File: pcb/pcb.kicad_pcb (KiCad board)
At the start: 2 copper layers, 2 parts

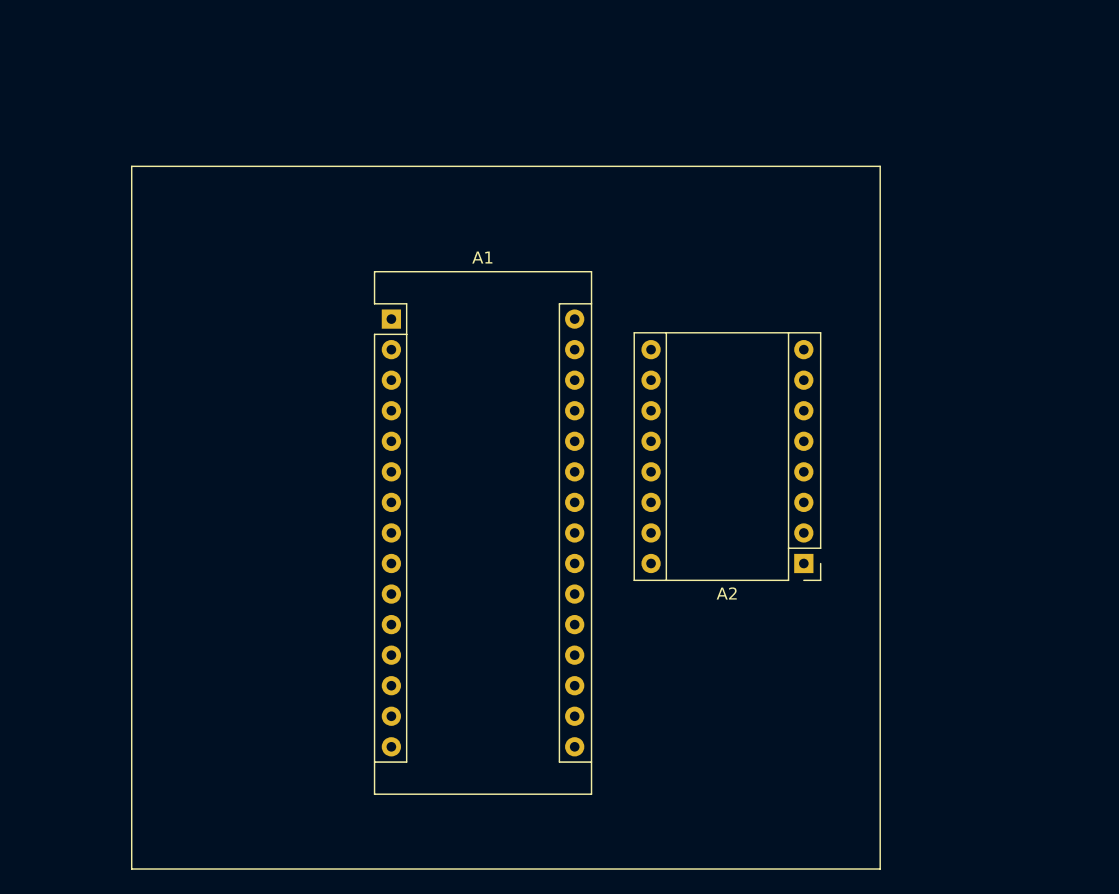
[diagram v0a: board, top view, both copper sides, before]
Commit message: add display support
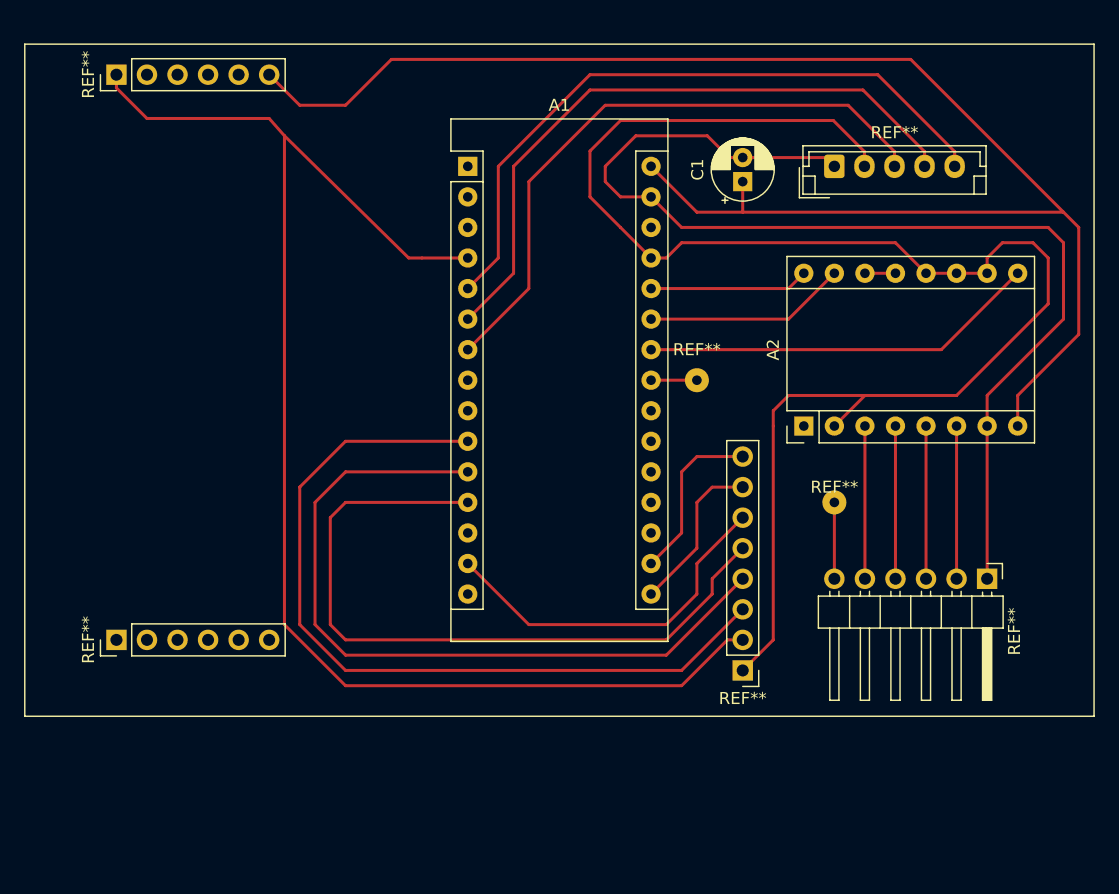
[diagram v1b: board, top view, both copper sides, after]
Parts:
- added C1: CP, Capacitor_THT:CP_Radial_D5.0mm_P2.00mm, F.Cu at (105.4, 52.1)
- added REF**: PinHeader_1x06, Connector_PinHeader_2.54mm:PinHeader_1x06_P2.54mm_Vertical, F.Cu at (53.3, 90.2)
- added REF**: PinHeader_1x06, Connector_PinHeader_2.54mm:PinHeader_1x06_P2.54mm_Vertical, F.Cu at (53.3, 43.2)
- added REF**: pad, Connector_Wire:SolderWirePad_1x01_Drill0.8mm, F.Cu at (101.6, 68.6)
- added REF**: pad, Connector_Wire:SolderWirePad_1x01_Drill0.8mm, F.Cu at (113.0, 78.7)
- added REF**: PinHeader, Connector_PinHeader_2.54mm:PinHeader_1x08_P2.54mm_Vertical, F.Cu at (105.4, 92.7)
- added REF**: JST_5, Connector_JST:JST_EH_B5B-EH-A_1x05_P2.50mm_Vertical, F.Cu at (113.0, 50.8)
- added REF**: PinHeader, Connector_PinHeader_2.54mm:PinHeader_1x06_P2.54mm_Horizontal, F.Cu at (125.7, 85.1)
- A1: value Arduino_Nano_v3.x -> Nano_v3.x
- A2: value Pololu_Breakout_A4988 -> A4988
- moved A1 14.2 mm to (82.5, 50.8)
- moved A2 11.4 mm to (110.5, 72.4), turned to 90 degrees
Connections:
- A1 pad 10: Net-(A1-Pad10) -> tft_CS
- A1 pad 11: Net-(A1-Pad11) -> tft_RES
- A1 pad 12: Net-(A1-Pad12) -> tft_A0
- A1 pad 14: Net-(A1-Pad14) -> tft_SDA
- A1 pad 16: Net-(A1-Pad16) -> tft_SCK
- A1 pad 17: Net-(A1-Pad17) -> tft_LED
- A1 pad 19: encoder_sw -> Net-(A1-Pad19)
- A1 pad 20: encoder_dt -> Net-(A1-Pad20)
- A1 pad 21: encoder_clk -> Net-(A1-Pad21)
- A1 pad 25: end_signal -> Net-(A1-Pad25)
- A1 pad 27: encoder_Vcc -> ardu_5V
- A1 pad 4: Net-(A1-Pad4) -> ardu_gnd2
- A1 pad 5: Net-(A1-Pad5) -> encoder_dt
- A1 pad 6: Net-(A1-Pad6) -> encoder_clk
- A1 pad 7: Net-(A1-Pad7) -> encoder_sw
- A2 pad 1: ardu_gnd -> Net-(A2-Pad1)
- A2 pad 10: ardu_gnd -> ardu_5V
- A2 pad 11: ardu_gnd -> ardu_5V
- A2 pad 12: ardu_gnd -> ardu_5V
- A2 pad 15: Net-(A1-Pad23) -> Net-(A1-Pad25)
- A2 pad 16: Net-(A1-Pad24) -> Net-(A2-Pad16)
- A2 pad 2: encoder_Vcc -> ardu_5V
- A2 pad 6: Net-(A2-Pad6) -> stepper_2B
- A2 pad 7: Net-(A2-Pad7) -> ardu_gnd
- A2 pad 9: Net-(A1-Pad22) -> Net-(A1-Pad24)
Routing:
- net ardu_vcc: track 0.00 -> 132.7 mm
- net ardu_5v: track 0.00 -> 130.7 mm
- net ardu_gnd2: track 0.00 -> 118.6 mm
- net ardu_gnd: track 0.00 -> 93.2 mm
- net tft_CS: track 0.00 -> 67.5 mm
- net tft_RES: track 0.00 -> 63.2 mm
- net tft_A0: track 0.00 -> 59.6 mm
- net encoder_dt: track 0.00 -> 56.2 mm
- net encoder_clk: track 0.00 -> 54.4 mm
- net encoder_sw: track 0.00 -> 51.9 mm
- net Net-(A1-Pad24): track 0.00 -> 33.1 mm
- net tft_SDA: track 0.00 -> 30.1 mm
- net Net-(A1-Pad25): track 0.00 -> 16.8 mm
- net tft_LED: track 0.00 -> 14.3 mm
- net tft_SCK: track 0.00 -> 13.5 mm
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
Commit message: update pcb
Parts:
- removed the REF** at (53.3, 90.2)
- removed the REF** at (53.3, 43.2)
- removed the REF** at (105.4, 92.7)
- added Q1: 2N3906, Package_TO_SOT_THT:TO-92_Inline, F.Cu at (123.2, 66.0)
- added R1: R, Resistor_THT:R_Axial_DIN0204_L3.6mm_D1.6mm_P5.08mm_Horizontal, F.Cu at (123.2, 69.2)
- added REF**: PinHeader_1x02_P2.54mm_Horizontal, Connector_PinHeader_2.54mm:PinHeader_1x02_P2.54mm_Horizontal, F.Cu at (70.5, 68.6)
- added REF**: PinSocket_1x08_P2.54mm_Vertical, Connector_PinSocket_2.54mm:PinSocket_1x08_P2.54mm_Vertical, F.Cu at (104.1, 94.0)
- added REF**: PinHeader_1x08_P2.54mm_Horizontal, Connector_PinHeader_2.54mm:PinHeader_1x08_P2.54mm_Horizontal, F.Cu at (59.7, 59.7)
- added REF**: JST_1x02, Connector_JST:JST_EH_B2B-EH-A_1x02_P2.50mm_Vertical, F.Cu at (82.5, 43.2)
- added REF**: pad, Connector_Wire:SolderWirePad_1x01_Drill0.8mm, F.Cu at (110.5, 68.6)
- added REF**: pad, Connector_Wire:SolderWirePad_1x01_Drill0.8mm, F.Cu at (105.4, 68.6)
- moved REF** 5.85 mm to (121.3, 81.3)
- moved REF** 5.24 mm to (100.3, 73.7)
- moved REF** 4.84 mm to (108.6, 76.8)
- moved A2 4.44 mm to (106.0, 72.4)
- moved A1 1.27 mm to (81.3, 50.8)
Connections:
- A2 pad 15: Net-(A1-Pad25) -> Net-(A1-Pad23)
- A2 pad 16: Net-(A2-Pad16) -> Net-(A1-Pad24)
- A2 pad 9: Net-(A1-Pad24) -> Net-(A1-Pad20)
- REF** pad 1: Net-(A1-Pad23) -> Net-(A1-Pad21)
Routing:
- net ardu_5v: track 130.7 -> 37.9 mm
- net ardu_5V: track 0.00 -> 72.9 mm
- net ardu_gnd2: track 118.6 -> 69.2 mm
- net Net-(A1-Pad20): track 0.00 -> 35.7 mm
- net (no net): track 0.00 -> 35.7 mm
- net ardu_vcc: track 132.7 -> 103.1 mm
- net Net-(A1-Pad24): track 33.1 -> 12.2 mm
- net tft_A0: track 59.6 -> 40.5 mm
- net tft_RES: track 63.2 -> 45.6 mm
- net Net-(A1-Pad25): track 16.8 -> 0.00 mm
- net tft_CS: track 67.5 -> 51.4 mm
- net Net-(A1-Pad26): track 13.2 -> 0.00 mm
- net Net-(A1-Pad23): track 3.81 -> 15.7 mm
- net ardu_gnd: track 93.2 -> 83.4 mm
- net stepper_2B: track 12.7 -> 8.89 mm
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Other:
- board outline added: 72.4 x 55.9 mm

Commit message: update pcb
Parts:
- added REF**: 0.8mm, Connector_Wire:SolderWirePad_1x01_Drill0.8mm, F.Cu at (59.1, 42.5)
- added REF**: ., Connector_Wire:SolderWirePad_1x01_Drill0.8mm, F.Cu at (125.7, 42.5)
- added REF**: ., Connector_Wire:SolderWirePad_1x01_Drill0.8mm, F.Cu at (125.7, 92.1)
- added REF**: 0.8mm, Connector_Wire:SolderWirePad_1x01_Drill0.8mm, F.Cu at (59.1, 92.1)
- moved REF** 1.27 mm to (82.5, 41.9)
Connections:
- REF** pad 1: (no net) -> ardu_vcc
- REF** pad 2: ardu_vcc -> (no net)
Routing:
- net (no net): track 35.7 -> 111.8 mm
- net ardu_vcc: track 103.1 -> 135.9 mm
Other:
- board size 72.4 x 55.9 mm -> 73 x 55.9 mm
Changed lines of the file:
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@@
     (thickness 1.6)
     (drawings 4)
-    (tracks 151)
+    (tracks 169)
     (zones 0)
-    (modules 15)
+    (modules 19)
     (nets 39)
   )
@@
     (add_net tft_SCK)
     (add_net tft_SDA)
+  )
+  (module Connector_Wire:SolderWirePad_1x01_Drill0.8mm (layer F.Cu)
+    (at 59.055 42.545)
+    (descr "Wire solder connection")
+    (tags connector)
+    (attr virtual)
+    (fp_text reference REF** (at 0 -2.54) (layer F.SilkS)
+      (effects (font (size 1 1) (thickness 0.15)))
+    )
+    (fp_text value 0.8mm (at 0 2.54) (layer F.Fab)
+      (effects (font (size 1 1) (thickness 0.15)))
+    )
+    (fp_text user %R (at 0 0) (layer F.Fab)
+      (effects (font (size 1 1) (thickness 0.15)))
+    )
+    (fp_line (start -1.5 -1.5) (end 1.5 -1.5) (layer F.CrtYd) (width 0.05))
+    (fp_line (start -1.5 -1.5) (end -1.5 1.5) (layer F.CrtYd) (width 0.05))
+    (fp_line (start 1.5 1.5) (end 1.5 -1.5) (layer F.CrtYd) (width 0.05))
+    (fp_line (start 1.5 1.5) (end -1.5 1.5) (layer F.CrtYd) (width 0.05))
+    (pad 1 thru_hole circle (at 0 0) (size 1.99898 1.99898) (drill 0.8001) (layers *.Cu *.Mask))
+  )
+  (module Connector_Wire:SolderWirePad_1x01_Drill0.8mm (layer F.Cu)
+    (at 125.73 42.545)
+    (descr "Wire solder connection")
+    (tags connector)
+    (attr virtual)
+    (fp_text reference REF** (at 0 -2.54) (layer F.SilkS)
+      (effects (font (size 1 1) (thickness 0.15)))
+    )
+    (fp_text value . (at 0 2.54) (layer F.Fab)
+      (effects (font (size 1 1) (thickness 0.15)))
+    )
+    (fp_line (start 1.5 1.5) (end -1.5 1.5) (layer F.CrtYd) (width 0.05))
+    (fp_line (start 1.5 1.5) (end 1.5 -1.5) (layer F.CrtYd) (width 0.05))
+    (fp_line (start -1.5 -1.5) (end -1.5 1.5) (layer F.CrtYd) (width 0.05))
+    (fp_line (start -1.5 -1.5) (end 1.5 -1.5) (layer F.CrtYd) (width 0.05))
+    (fp_text user %R (at 0 0) (layer F.Fab)
+      (effects (font (size 1 1) (thickness 0.15)))
+    )
+    (pad 1 thru_hole circle (at 0 0) (size 1.99898 1.99898) (drill 0.8001) (layers *.Cu *.Mask))
+  )
+  (module Connector_Wire:SolderWirePad_1x01_Drill0.8mm (layer F.Cu)
+    (at 125.73 92.075)
+    (descr "Wire solder connection")
+    (tags connector)
+    (attr virtual)
+    (fp_text reference REF** (at 0 -2.54) (layer F.SilkS)
+      (effects (font (size 1 1) (thickness 0.15)))
+    )
+    (fp_text value . (at 0 2.54) (layer F.Fab)
+      (effects (font (size 1 1) (thickness 0.15)))
+    )
+    (fp_text user %R (at 0 0) (layer F.Fab)
+      (effects (font (size 1 1) (thickness 0.15)))
+    )
+    (fp_line (start -1.5 -1.5) (end 1.5 -1.5) (layer F.CrtYd) (width 0.05))
+    (fp_line (start -1.5 -1.5) (end -1.5 1.5) (layer F.CrtYd) (width 0.05))
+    (fp_line (start 1.5 1.5) (end 1.5 -1.5) (layer F.CrtYd) (width 0.05))
+    (fp_line (start 1.5 1.5) (end -1.5 1.5) (layer F.CrtYd) (width 0.05))
+    (pad 1 thru_hole circle (at 0 0) (size 1.99898 1.99898) (drill 0.8001) (layers *.Cu *.Mask))
+  )
+  (module Connector_Wire:SolderWirePad_1x01_Drill0.8mm (layer F.Cu)
+    (at 59.055 92.075)
+    (descr "Wire solder connection")
+    (tags connector)
+    (attr virtual)
+    (fp_text reference REF** (at 0 -2.54) (layer F.SilkS)
+      (effects (font (size 1 1) (thickness 0.15)))
+    )
+    (fp_text value 0.8mm (at 0 2.54) (layer F.Fab)
+      (effects (font (size 1 1) (thickness 0.15)))
+    )
+    (fp_line (start 1.5 1.5) (end -1.5 1.5) (layer F.CrtYd) (width 0.05))
+    (fp_line (start 1.5 1.5) (end 1.5 -1.5) (layer F.CrtYd) (width 0.05))
+    (fp_line (start -1.5 -1.5) (end -1.5 1.5) (layer F.CrtYd) (width 0.05))
+    (fp_line (start -1.5 -1.5) (end 1.5 -1.5) (layer F.CrtYd) (width 0.05))
+    (fp_text user %R (at 0 0) (layer F.Fab)
+      (effects (font (size 1 1) (thickness 0.15)))
+    )
+    (pad 1 thru_hole circle (at 0 0) (size 1.99898 1.99898) (drill 0.8001) (layers *.Cu *.Mask))
   )
   (module Connector_PinHeader_2.54mm:PinHeader_1x02_P2.54mm_Horizontal (layer F.Cu)
@@
     (pad 3 thru_hole oval (at 0 5.08 90) (size 1.7 1.7) (drill 1) (layers *.Cu *.Mask))
     (pad 2 thru_hole oval (at 0 2.54 90) (size 1.7 1.7) (drill 1) (layers *.Cu *.Mask))
-    (pad 1 thru_hole rect (at 0 0 90) (size 1.7 1.7) (drill 1) (layers *.Cu *.Mask))
+    (pad 1 thru_hole rect (at 0 0 90) (size 1.7 1.7) (drill 1) (layers *.Cu *.Mask)
+      (net 14 ardu_vcc))
     (model ${KISYS3DMOD}/Connector_PinHeader_2.54mm.3dshapes/PinHeader_1x08_P2.54mm_Horizontal.wrl
       (at (xyz 0 0 0))
@@
   )
   (module Connector_JST:JST_EH_B2B-EH-A_1x02_P2.50mm_Vertical (layer F.Cu)
-    (at 82.55 43.18)
+    (at 82.55 41.91)
     (descr "JST EH series connector, B2B-EH-A (http://www.jst-mfg.com/product/pdf/eng/eEH.pdf), generated with kicad-footprint-generator")
     (tags "connector JST EH vertical")
@@
     (fp_line (start -2.5 2.2) (end 5 2.2) (layer F.Fab) (width 0.1))
     (fp_line (start -2.5 -1.6) (end -2.5 2.2) (layer F.Fab) (width 0.1))
-    (pad 2 thru_hole oval (at 2.5 0) (size 1.7 2) (drill 1) (layers *.Cu *.Mask)
-      (net 14 ardu_vcc))
+    (pad 2 thru_hole oval (at 2.5 0) (size 1.7 2) (drill 1) (layers *.Cu *.Mask))
     (pad 1 thru_hole roundrect (at 0 0) (size 1.7 2) (drill 1) (layers *.Cu *.Mask) (roundrect_rratio 0.147))
     (model ${KISYS3DMOD}/Connector_JST.3dshapes/JST_EH_B2B-EH-A_1x02_P2.50mm_Vertical.wrl
@@
   )
   (gr_line (start 55.88 95.25) (end 55.88 39.37) (layer Edge.Cuts) (width 0.05))
-  (gr_line (start 128.27 95.25) (end 55.88 95.25) (layer Edge.Cuts) (width 0.05))
-  (gr_line (start 128.27 39.37) (end 128.27 95.25) (layer Edge.Cuts) (width 0.05))
-  (gr_line (start 55.88 39.37) (end 128.27 39.37) (layer Edge.Cuts) (width 0.05))
-  (segment (start 59.69 59.69) (end 59.69 49.53) (width 0.25) (layer F.Cu) (net 0))
-  (segment (start 66.04 43.18) (end 82.55 43.18) (width 0.25) (layer F.Cu) (net 0))
-  (segment (start 59.69 49.53) (end 66.04 43.18) (width 0.25) (layer F.Cu) (net 0))
+  (gr_line (start 128.905 95.25) (end 55.88 95.25) (layer Edge.Cuts) (width 0.05))
+  (gr_line (start 128.905 39.37) (end 128.905 95.25) (layer Edge.Cuts) (width 0.05))
+  (gr_line (start 55.88 39.37) (end 128.905 39.37) (layer Edge.Cuts) (width 0.05))
+  (segment (start 72.39 60.892081) (end 72.39 59.69) (width 0.25) (layer F.Cu) (net 0))
+  (segment (start 72.39 67.775) (end 72.39 60.892081) (width 0.25) (layer F.Cu) (net 0))
+  (segment (start 71.585 68.58) (end 72.39 67.775) (width 0.25) (layer F.Cu) (net 0))
+  (segment (start 70.485 68.58) (end 71.585 68.58) (width 0.25) (layer F.Cu) (net 0))
+  (segment (start 67.945 68.58) (end 62.23 68.58) (width 0.25) (layer F.Cu) (net 0))
+  (segment (start 62.23 68.58) (end 57.15 63.5) (width 0.25) (layer F.Cu) (net 0))
+  (segment (start 82.55 41.91) (end 68.58 41.91) (width 0.25) (layer F.Cu) (net 0))
+  (segment (start 68.58 41.91) (end 57.15 53.34) (width 0.25) (layer F.Cu) (net 0))
+  (segment (start 85.05 43.16) (end 84.395 43.815) (width 0.25) (layer F.Cu) (net 0))
+  (segment (start 85.05 41.91) (end 85.05 43.16) (width 0.25) (layer F.Cu) (net 0))
+  (segment (start 84.395 43.815) (end 72.39 43.815) (width 0.25) (layer F.Cu) (net 0))
+  (segment (start 72.39 43.815) (end 57.785 58.42) (width 0.25) (layer F.Cu) (net 0))
+  (segment (start 57.785 58.42) (end 57.785 62.23) (width 0.25) (layer F.Cu) (net 0))
+  (segment (start 57.785 62.23) (end 59.055 63.5) (width 0.25) (layer F.Cu) (net 0))
+  (segment (start 60.96 63.5) (end 64.77 59.69) (width 0.25) (layer F.Cu) (net 0))
+  (segment (start 59.055 63.5) (end 60.96 63.5) (width 0.25) (layer F.Cu) (net 0))
+  (segment (start 57.15 53.34) (end 56.515 53.975) (width 0.25) (layer F.Cu) (net 0))
+  (segment (start 56.515 53.975) (end 56.515 62.865) (width 0.25) (layer F.Cu) (net 0))
+  (segment (start 56.515 62.865) (end 57.15 63.5) (width 0.25) (layer F.Cu) (net 0))
   (segment (start 99.695 66.04) (end 106.045 59.69) (width 0.25) (layer F.Cu) (net 6))
   (segment (start 96.52 66.04) (end 99.695 66.04) (width 0.25) (layer F.Cu) (net 6))
@@
   (segment (start 101.6 54.61) (end 105.41 54.61) (width 0.25) (layer F.Cu) (net 14))
   (segment (start 97.79 50.8) (end 96.52 50.8) (width 0.25) (layer F.Cu) (net 14))
-  (segment (start 123.19 54.61) (end 125.73 52.07) (width 0.25) (layer F.Cu) (net 14))
   (segment (start 105.41 54.61) (end 123.19 54.61) (width 0.25) (layer F.Cu) (net 14))
-  (segment (start 125.73 52.07) (end 125.73 49.53) (width 0.25) (layer F.Cu) (net 14))
-  (segment (start 118.11 41.91) (end 125.73 49.53) (width 0.25) (layer F.Cu) (net 14))
-  (segment (start 85.05 43.18) (end 91.44 43.18) (width 0.25) (layer F.Cu) (net 14))
-  (segment (start 91.44 43.18) (end 92.71 41.91) (width 0.25) (layer F.Cu) (net 14))
-  (segment (start 118.11 41.91) (end 92.71 41.91) (width 0.25) (layer F.Cu) (net 14))
   (segment (start 125.095 54.61) (end 127 56.515) (width 0.25) (layer F.Cu) (net 14))
   (segment (start 123.19 54.61) (end 125.095 54.61) (width 0.25) (layer F.Cu) (net 14))
   (segment (start 127 69.215) (end 123.825 72.39) (width 0.25) (layer F.Cu) (net 14))
   (segment (start 127 56.515) (end 127 69.215) (width 0.25) (layer F.Cu) (net 14))
+  (segment (start 125.73 52.07) (end 123.19 54.61) (width 0.25) (layer F.Cu) (net 14))
+  (segment (start 125.73 49.53) (end 125.73 52.07) (width 0.25) (layer F.Cu) (net 14))
+  (segment (start 118.11 41.91) (end 125.73 49.53) (width 0.25) (layer F.Cu) (net 14))
+  (segment (start 59.69 58.59) (end 72.56 45.72) (width 0.25) (layer F.Cu) (net 14))
+  (segment (start 72.56 45.72) (end 88.9 45.72) (width 0.25) (layer F.Cu) (net 14))
+  (segment (start 59.69 59.69) (end 59.69 58.59) (width 0.25) (layer F.Cu) (net 14))
+  (segment (start 88.9 45.72) (end 92.71 41.91) (width 0.25) (layer F.Cu) (net 14))
+  (segment (start 92.71 41.91) (end 118.11 41.91) (width 0.25) (layer F.Cu) (net 14))
   (segment (start 112.3 50.07) (end 113.03 50.8) (width 0.25) (layer F.Cu) (net 15))
   (segment (start 105.41 50.07) (end 112.3 50.07) (width 0.25) (layer F.Cu) (net 15))
